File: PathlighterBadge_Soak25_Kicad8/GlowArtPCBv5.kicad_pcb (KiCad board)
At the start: 2 copper layers, 135.4 x 115.3 mm, 7 parts, among them SW1 SW_SPDT

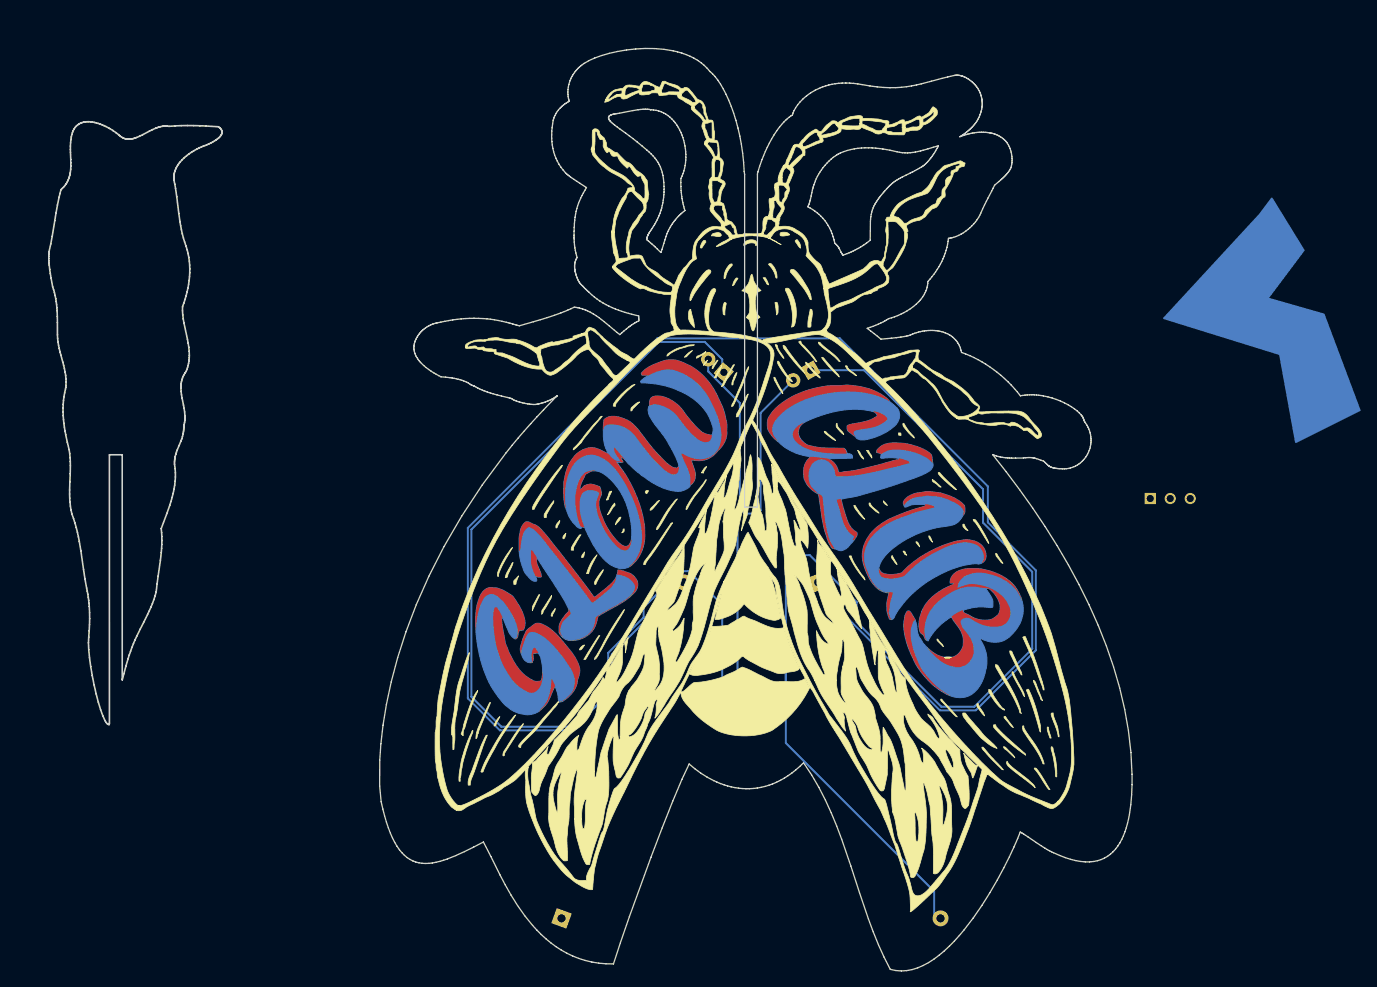
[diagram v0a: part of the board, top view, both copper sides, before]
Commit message: Add SVGs and update board
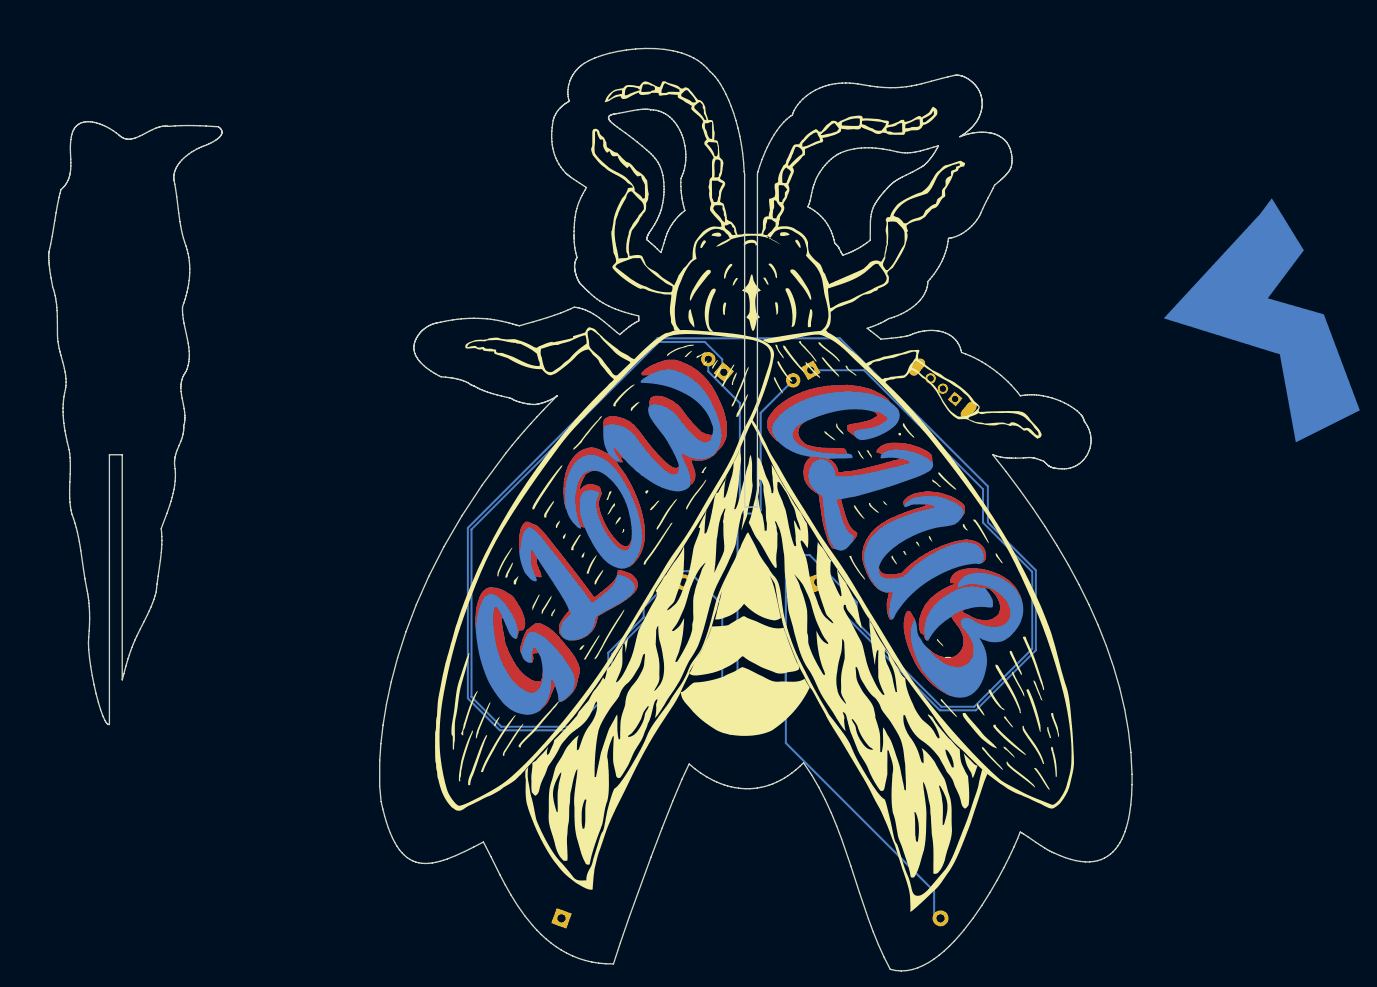
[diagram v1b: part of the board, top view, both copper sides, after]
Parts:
- removed the flat side at (201.2, 125.7)
- removed the flat side at (207.9, 81.5)
- added flat side: LED, LED_THT:LED_D5.0mm_Horizontal_O1.27mm_Z3.0mm, B.Cu at (201.2, 125.7)
- added flat side: LED, LED_THT:LED_D5.0mm_Horizontal_O1.27mm_Z3.0mm, B.Cu at (207.9, 81.5)
- SW1: footprint Button_Switch_THT:SW_MHSS1105_SPST_Angled -> Local Footprints:SW_SS12D07VG4
- moved SW1 29.3 mm to (224.4, 83.8), turned to 140 degrees

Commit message: Remove old design
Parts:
- removed REF**: MountingHole_3mm, MountingHole:MountingHole_3mm
- removed the flat side at (201.2, 125.7)
- removed the flat side at (207.9, 81.5)
- added flat side: LED, LED_THT:LED_D5.0mm_Horizontal_O1.27mm_Z3.0mm, B.Cu at (207.9, 81.5)
- added flat side: LED, LED_THT:LED_D5.0mm_Horizontal_O1.27mm_Z3.0mm, B.Cu at (201.2, 125.7)
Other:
- board outline removed
- board text removed: "Let your light shine so brightly that you illuminate a pathway for others to find their way out of the darkness"
- board text removed: "design files: Github.com/Drc3p0"

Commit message: Update for V1
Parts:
- removed the flat side at (207.9, 81.5)
- removed the flat side at (197.0, 81.8)
- removed the flat side at (201.2, 125.7)
- added ? (x5): , Graphics, F.Cu at (154.4, 41.5)
- added ?: , Graphics, B.Cu at (154.4, 41.5)
- added flat side: LED, LED_THT:LED_D5.0mm_Horizontal_O1.27mm_Z3.0mm, B.Cu at (197.0, 81.8)
- added flat side: LED, LED_THT:LED_D5.0mm_Horizontal_O1.27mm_Z3.0mm, B.Cu at (201.2, 125.7)
- added flat side: LED, LED_THT:LED_D5.0mm_Horizontal_O1.27mm_Z3.0mm, B.Cu at (207.9, 81.5)
- moved BT2 47.1 mm to (223.8, 151.2), turned to 110 degrees
- moved BT1 16.1 mm to (192.8, 109.2), turned to -110 degrees
- moved SW1 0.21 mm to (224.2, 83.7)
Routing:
- net Net-(BT1-Pad1): track 203.5 -> 15.7 mm
- net Net-(BT1-Pad2): track 287.7 -> 109.0 mm
- net Net-(BT2-Pad1): track 0.00 -> 78.4 mm
- net Net-(D1-Pad2): track 74.5 -> 88.8 mm
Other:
- board outline added: 93.2 x 113.9 mm

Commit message: Add silkscreen text
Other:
- board text added: "Let your light shine so brightly that you illuminate a pathway for others to find their way out of the darkness"
- board text added: "design files: Github.com/Drc3p0"
